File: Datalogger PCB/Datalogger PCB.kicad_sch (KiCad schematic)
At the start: 45 parts, among them J1 Conn_01x02_Pin, M1 Motor_Servo, M2 Motor_Servo, M3 Motor_Servo, M4 Motor_Servo, U1 Teensy4.1, U2 BNO055, U3 LPS25HB, U4 AMS1117-5.0, U5 NRF24L01_Breakout, U6 VN5E160STR-E, U7 VN5E160STR-E, U8 VN5E160STR-E, U9 VN5E160STR-E

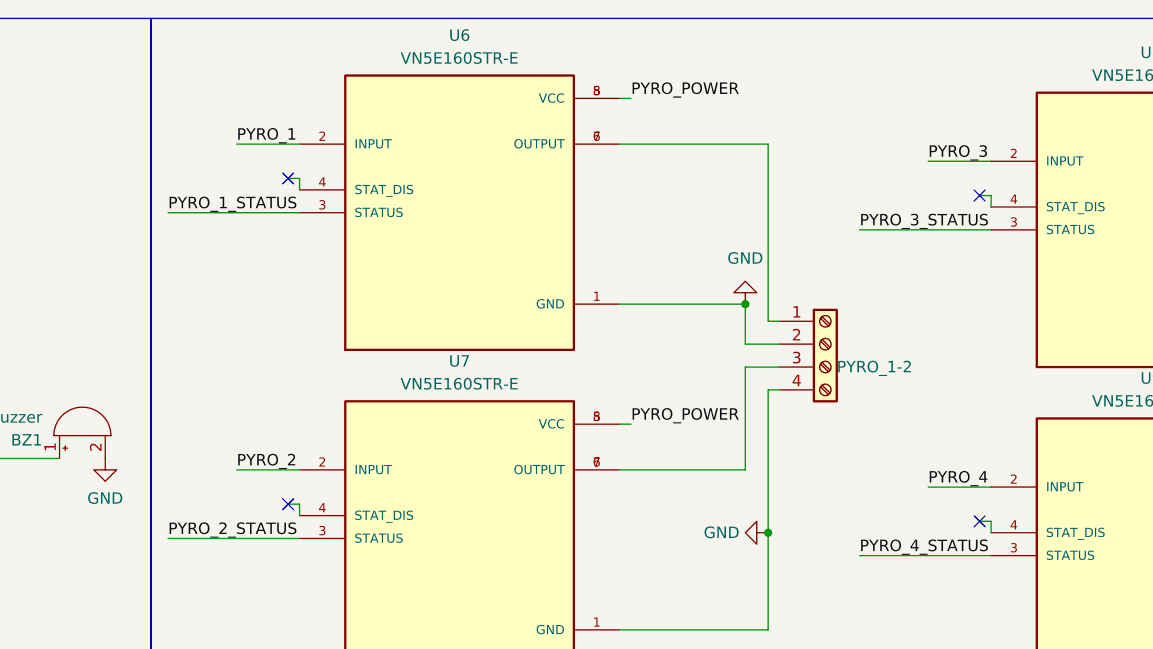
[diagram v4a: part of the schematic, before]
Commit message: Added pull down resistor to pyro channels
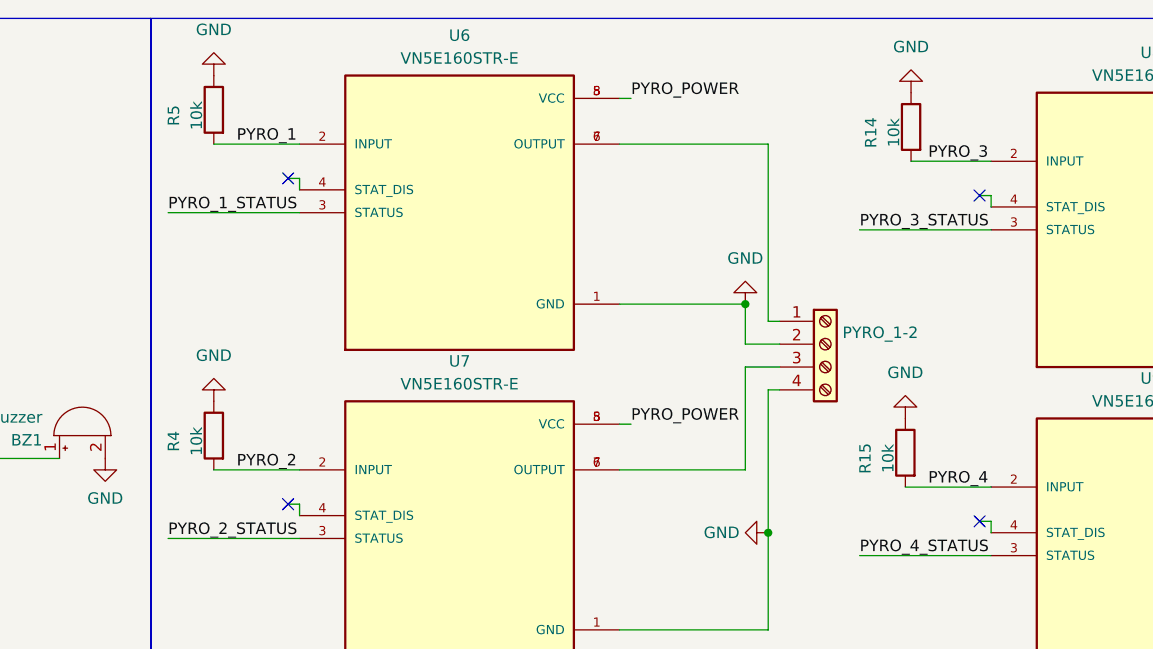
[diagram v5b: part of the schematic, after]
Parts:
- added R14, R15, R4, R5: 10k, Resistor_SMD:R_0603_1608Metric_Pad0.98x0.95mm_HandSolder, symbol Device:R
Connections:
- net GND: now also R14.1, R15.1, R4.1, R5.1
- net PYRO_1: now also R5.2
- net PYRO_2: now also R4.2
- net PYRO_3: now also R14.2
- net PYRO_4: now also R15.2
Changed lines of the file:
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@@
     (stroke (width 0) (type default))
   )
-  (wire (pts (xy 219.71 64.135) (xy 226.695 64.135))
+  (wire (pts (xy 217.17 64.135) (xy 226.695 64.135))
     (stroke (width 0) (type default))
   )
@@
     (stroke (width 0) (type default))
   )
-  (wire (pts (xy 142.875 26.035) (xy 149.86 26.035))
+  (wire (pts (xy 140.335 26.035) (xy 149.86 26.035))
     (stroke (width 0) (type default))
   )
@@
     (stroke (width 0) (type default))
   )
-  (wire (pts (xy 142.875 62.23) (xy 149.86 62.23))
+  (wire (pts (xy 140.335 62.23) (xy 149.86 62.23))
     (stroke (width 0) (type default))
   )
@@
     (stroke (width 0) (type default))
   )
-  (wire (pts (xy 219.71 27.94) (xy 226.695 27.94))
+  (wire (pts (xy 217.805 27.94) (xy 226.695 27.94))
     (stroke (width 0) (type default))
   )
@@
     )
   )
+  (symbol (lib_id "Device:R") (at 140.335 58.42 0) (mirror y) (unit 1)
+    (in_bom yes) (on_board yes) (dnp no)
+    (property "Reference" "R4" (at 135.89 59.055 90)
+      (effects (font (size 1.27 1.27)))
+    )
+    (property "Value" "10k" (at 138.43 59.055 90)
+      (effects (font (size 1.27 1.27)))
+    )
+    (property "Footprint" "Resistor_SMD:R_0603_1608Metric_Pad0.98x0.95mm_HandSolder" (at 142.113 58.42 90)
+      (effects (font (size 1.27 1.27)) hide)
+    )
+    (property "Datasheet" "~" (at 140.335 58.42 0)
+      (effects (font (size 1.27 1.27)) hide)
+    )
+    (pin "1")
+    (pin "2")
+    (instances
+      (project "Datalogger PCB"
+        (path "/a3bc5533-d6ac-45b5-a7d9-fc1b12646794"
+          (reference "R4") (unit 1)
+        )
+      )
+    )
+  )
   (symbol (lib_id "Device:R") (at 190.5 190.5 180) (unit 1)
     (in_bom yes) (on_board yes) (dnp no)
@@
     )
   )
+  (symbol (lib_id "Device:R") (at 217.805 24.13 0) (mirror y) (unit 1)
+    (in_bom yes) (on_board yes) (dnp no)
+    (property "Reference" "R14" (at 213.36 24.765 90)
+      (effects (font (size 1.27 1.27)))
+    )
+    (property "Value" "10k" (at 215.9 24.765 90)
+      (effects (font (size 1.27 1.27)))
+    )
+    (property "Footprint" "Resistor_SMD:R_0603_1608Metric_Pad0.98x0.95mm_HandSolder" (at 219.583 24.13 90)
+      (effects (font (size 1.27 1.27)) hide)
+    )
+    (property "Datasheet" "~" (at 217.805 24.13 0)
+      (effects (font (size 1.27 1.27)) hide)
+    )
+    (pin "1")
+    (pin "2")
+    (instances
+      (project "Datalogger PCB"
+        (path "/a3bc5533-d6ac-45b5-a7d9-fc1b12646794"
+          (reference "R14") (unit 1)
+        )
+      )
+    )
+  )
   (symbol (lib_id "VN5E160STR-E:VN5E160STR-E") (at 244.475 71.755 0) (unit 1)
     (in_bom yes) (on_board yes) (dnp no)
@@
     )
   )
+  (symbol (lib_id "Device:R") (at 217.17 60.325 0) (mirror y) (unit 1)
+    (in_bom yes) (on_board yes) (dnp no)
+    (property "Reference" "R15" (at 212.725 60.96 90)
+      (effects (font (size 1.27 1.27)))
+    )
+    (property "Value" "10k" (at 215.265 60.96 90)
+      (effects (font (size 1.27 1.27)))
+    )
+    (property "Footprint" "Resistor_SMD:R_0603_1608Metric_Pad0.98x0.95mm_HandSolder" (at 218.948 60.325 90)
+      (effects (font (size 1.27 1.27)) hide)
+    )
+    (property "Datasheet" "~" (at 217.17 60.325 0)
+      (effects (font (size 1.27 1.27)) hide)
+    )
+    (pin "1")
+    (pin "2")
+    (instances
+      (project "Datalogger PCB"
+        (path "/a3bc5533-d6ac-45b5-a7d9-fc1b12646794"
+          (reference "R15") (unit 1)
+        )
+      )
+    )
+  )
   (symbol (lib_id "Motor:Motor_Servo") (at 317.5 87.63 0) (unit 1)
     (in_bom yes) (on_board yes) (dnp no) (fields_autoplaced)
@@
     )
   )
+  (symbol (lib_id "power:GND") (at 140.335 54.61 180) (unit 1)
+    (in_bom yes) (on_board yes) (dnp no) (fields_autoplaced)
+    (property "Reference" "#PWR04" (at 140.335 48.26 0)
+      (effects (font (size 1.27 1.27)) hide)
+    )
+    (property "Value" "GND" (at 140.335 49.53 0)
+      (effects (font (size 1.27 1.27)))
+    )
+    (property "Footprint" "" (at 140.335 54.61 0)
+      (effects (font (size 1.27 1.27)) hide)
+    )
+    (property "Datasheet" "" (at 140.335 54.61 0)
+      (effects (font (size 1.27 1.27)) hide)
+    )
+    (pin "1")
+    (instances
+      (project "Datalogger PCB"
+        (path "/a3bc5533-d6ac-45b5-a7d9-fc1b12646794"
+          (reference "#PWR04") (unit 1)
+        )
+      )
+    )
+  )
   (symbol (lib_id "power:+3.3V") (at 89.535 43.18 270) (unit 1)
     (in_bom yes) (on_board yes) (dnp no) (fields_autoplaced)
@@
   (symbol (lib_id "Connector:Screw_Terminal_01x04") (at 208.28 48.26 0) (unit 1)
     (in_bom yes) (on_board yes) (dnp no)
-    (property "Reference" "PYRO_1-2" (at 209.55 50.8 0)
+    (property "Reference" "PYRO_1-2" (at 210.185 46.99 0)
       (effects (font (size 1.27 1.27)) (justify left))
     )
@@
     )
   )
+  (symbol (lib_id "power:GND") (at 217.17 56.515 180) (unit 1)
+    (in_bom yes) (on_board yes) (dnp no) (fields_autoplaced)
+    (property "Reference" "#PWR053" (at 217.17 50.165 0)
+      (effects (font (size 1.27 1.27)) hide)
+    )
+    (property "Value" "GND" (at 217.17 51.435 0)
+      (effects (font (size 1.27 1.27)))
+    )
+    (property "Footprint" "" (at 217.17 56.515 0)
+      (effects (font (size 1.27 1.27)) hide)
+    )
+    (property "Datasheet" "" (at 217.17 56.515 0)
+      (effects (font (size 1.27 1.27)) hide)
+    )
+    (pin "1")
+    (instances
+      (project "Datalogger PCB"
+        (path "/a3bc5533-d6ac-45b5-a7d9-fc1b12646794"
+          (reference "#PWR053") (unit 1)
+        )
+      )
+    )
+  )
   (symbol (lib_id "power:+3.3V") (at 86.36 177.8 180) (unit 1)
     (in_bom yes) (on_board yes) (dnp no) (fields_autoplaced)
@@
         )
       )
+    )
+  )
+  (symbol (lib_id "power:GND") (at 217.805 20.32 180) (unit 1)
+    (in_bom yes) (on_board yes) (dnp no) (fields_autoplaced)
+    (property "Reference" "#PWR052" (at 217.805 13.97 0)
+      (effects (font (size 1.27 1.27)) hide)
+    )
+    (property "Value" "GND" (at 217.805 15.24 0)
+      (effects (font (size 1.27 1.27)))
+    )
+    (property "Footprint" "" (at 217.805 20.32 0)
+      (effects (font (size 1.27 1.27)) hide)
+    )
+    (property "Datasheet" "" (at 217.805 20.32 0)
+      (effects (font (size 1.27 1.27)) hide)
+    )
+    (pin "1")
+    (instances
+      (project "Datalogger PCB"
+        (path "/a3bc5533-d6ac-45b5-a7d9-fc1b12646794"
+          (reference "#PWR052") (unit 1)
+        )
+      )
+    )
+  )
+  (symbol (lib_id "Device:R") (at 140.335 22.225 0) (mirror y) (unit 1)
+    (in_bom yes) (on_board yes) (dnp no)
+    (property "Reference" "R5" (at 135.89 22.86 90)
+      (effects (font (size 1.27 1.27)))
+    )
+    (property "Value" "10k" (at 138.43 22.86 90)
+      (effects (font (size 1.27 1.27)))
+    )
+    (property "Footprint" "Resistor_SMD:R_0603_1608Metric_Pad0.98x0.95mm_HandSolder" (at 142.113 22.225 90)
+      (effects (font (size 1.27 1.27)) hide)
+    )
+    (property "Datasheet" "~" (at 140.335 22.225 0)
+      (effects (font (size 1.27 1.27)) hide)
+    )
+    (pin "1")
+    (pin "2")
+    (instances
+      (project "Datalogger PCB"
+        (path "/a3bc5533-d6ac-45b5-a7d9-fc1b12646794"
+          (reference "R5") (unit 1)
+        )
+      )
+    )
+  )
+  (symbol (lib_id "power:GND") (at 140.335 18.415 180) (unit 1)
+    (in_bom yes) (on_board yes) (dnp no) (fields_autoplaced)
+    (property "Reference" "#PWR08" (at 140.335 12.065 0)
+      (effects (font (size 1.27 1.27)) hide)
+    )
+    (property "Value" "GND" (at 140.335 13.335 0)
+      (effects (font (size 1.27 1.27)))
+    )
+    (property "Footprint" "" (at 140.335 18.415 0)
+      (effects (font (size 1.27 1.27)) hide)
+    )
+    (property "Datasheet" "" (at 140.335 18.415 0)
+      (effects (font (size 1.27 1.27)) hide)
+    )
+    (pin "1")
+    (instances
+      (project "Datalogger PCB"
+        (path "/a3bc5533-d6ac-45b5-a7d9-fc1b12646794"
+          (reference "#PWR08") (unit 1)
+        )
+      )

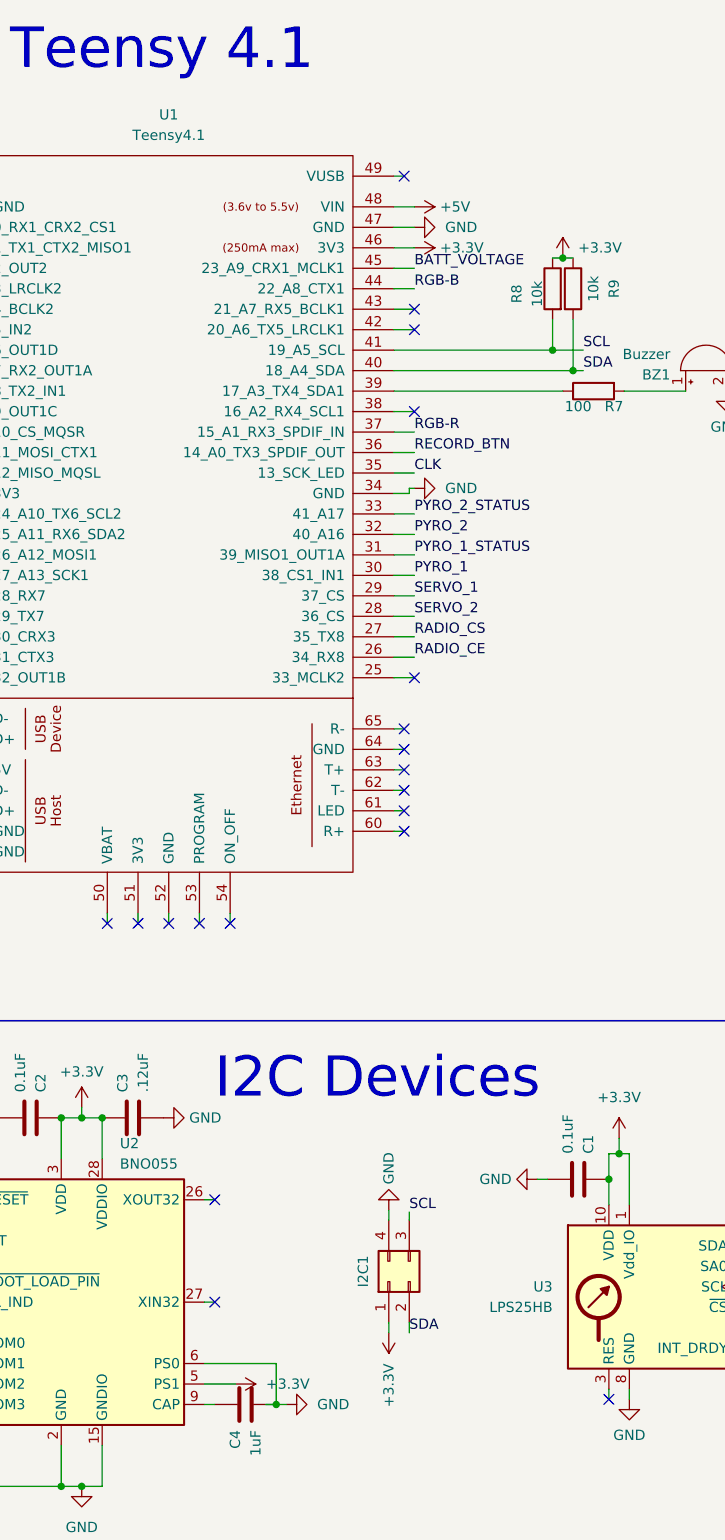
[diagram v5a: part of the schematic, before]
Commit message: Fixed a couple of pcb errors
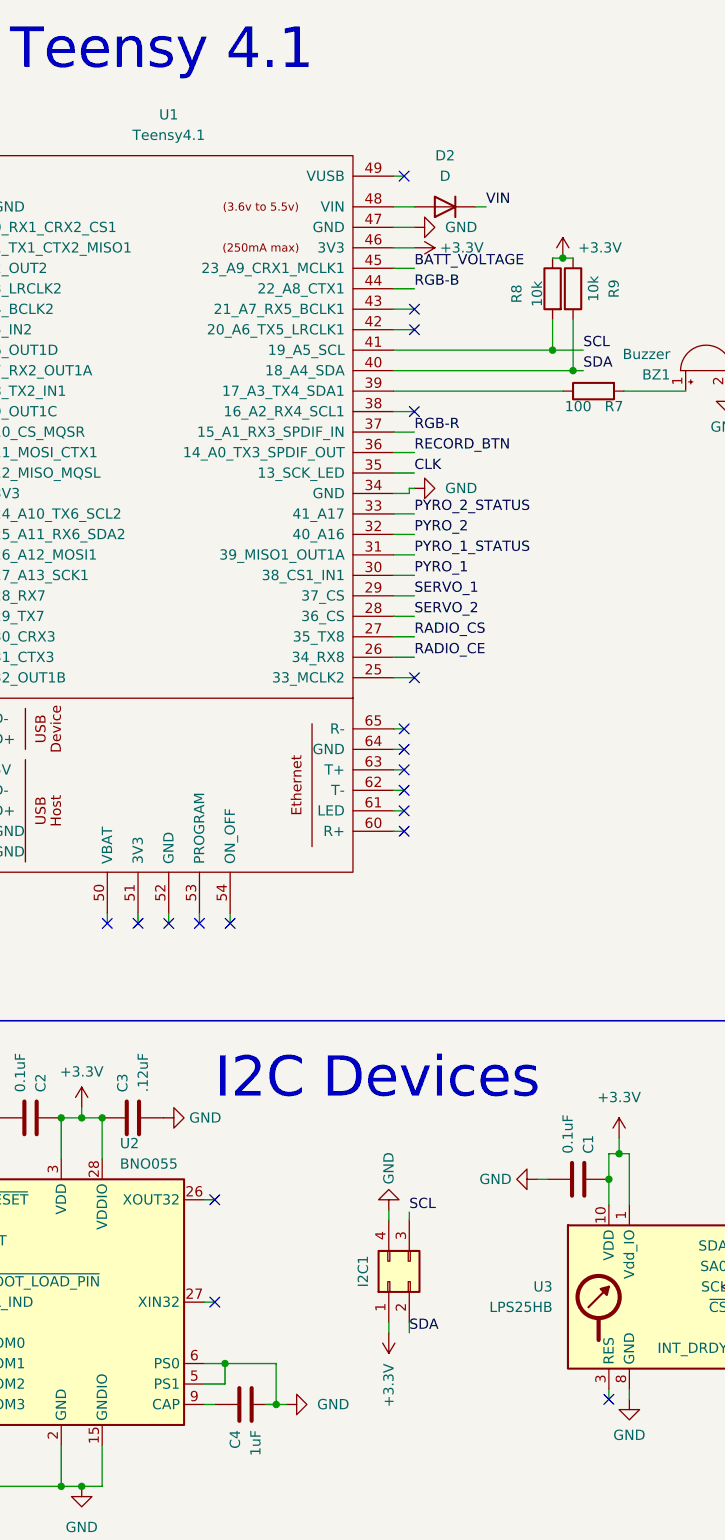
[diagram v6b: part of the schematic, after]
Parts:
- added D2: D, Diode_SMD:D_0603_1608Metric_Pad1.05x0.95mm_HandSolder, symbol Device:D
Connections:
- net +3.3V: no longer U2.5 (PS1)
- net +5V: no longer U1.48 (VIN)
- net GND: now also U2.5 (PS1)
- net VIN: now also D2.1 (K)
- new net: D2.2 (A), U1.48 (VIN)
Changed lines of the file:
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@@
   (junction (at 50.8 151.13) (diameter 0) (color 0 0 0 0)
   )
+  (junction (at 66.04 181.61) (diameter 0) (color 0 0 0 0)
+  )
   (junction (at 223.52 184.785) (diameter 0) (color 0 0 0 0)
   )
@@
     (stroke (width 0) (type default))
   )
-  (wire (pts (xy 63.5 181.61) (xy 72.39 181.61))
+  (wire (pts (xy 63.5 181.61) (xy 66.04 181.61))
     (stroke (width 0) (type default))
   )
@@
     (stroke (width 0) (type default))
   )
-  (wire (pts (xy 67.31 184.15) (xy 63.5 184.15))
-    (stroke (width 0) (type default))
-  )
   (wire (pts (xy 113.665 161.925) (xy 113.665 158.75))
     (stroke (width 0) (type default))
@@
     (stroke (width 0) (type default))
   )
+  (wire (pts (xy 66.04 181.61) (xy 72.39 181.61))
+    (stroke (width 0) (type default))
+  )
   (wire (pts (xy 89.535 88.9) (xy 86.995 88.9))
     (stroke (width 0) (type default))
@@
     (stroke (width 0) (type default))
   )
+  (wire (pts (xy 66.04 184.15) (xy 66.04 181.61))
+    (stroke (width 0) (type default))
+  )
   (wire (pts (xy 29.845 60.96) (xy 31.115 60.96))
     (stroke (width 0) (type default))
@@
     (stroke (width 0) (type default))
   )
+  (wire (pts (xy 63.5 184.15) (xy 66.04 184.15))
+    (stroke (width 0) (type default))
+  )
+  (wire (pts (xy 98.425 38.1) (xy 97.155 38.1))
+    (stroke (width 0) (type default))
+  )
   (wire (pts (xy 148.59 66.04) (xy 149.86 66.04))
     (stroke (width 0) (type default))
@@
     (effects (font (size 1.27 1.27)) (justify left bottom))
   )
+  (label "VIN" (at 98.425 38.1 0) (fields_autoplaced)
+    (effects (font (size 1.27 1.27)) (justify left bottom))
+  )
   (label "RADIO_CE" (at 89.535 93.98 0) (fields_autoplaced)
     (effects (font (size 1.27 1.27)) (justify left bottom))
@@
     )
   )
-  (symbol (lib_id "power:+5V") (at 89.535 38.1 270) (unit 1)
-    (in_bom yes) (on_board yes) (dnp no) (fields_autoplaced)
-    (property "Reference" "#PWR043" (at 85.725 38.1 0)
-      (effects (font (size 1.27 1.27)) hide)
-    )
-    (property "Value" "+5V" (at 92.71 38.1 90)
-      (effects (font (size 1.27 1.27)) (justify left))
-    )
-    (property "Footprint" "" (at 89.535 38.1 0)
-      (effects (font (size 1.27 1.27)) hide)
-    )
-    (property "Datasheet" "" (at 89.535 38.1 0)
-      (effects (font (size 1.27 1.27)) hide)
-    )
-    (pin "1")
-    (instances
-      (project "Datalogger PCB"
-        (path "/a3bc5533-d6ac-45b5-a7d9-fc1b12646794"
-          (reference "#PWR043") (unit 1)
-        )
-      )
-    )
-  )
   (symbol (lib_id "power:+5V") (at 224.79 184.785 270) (unit 1)
     (in_bom yes) (on_board yes) (dnp no) (fields_autoplaced)
@@
     )
   )
-  (symbol (lib_id "power:+3.3V") (at 67.31 184.15 270) (unit 1)
-    (in_bom yes) (on_board yes) (dnp no) (fields_autoplaced)
-    (property "Reference" "#PWR027" (at 63.5 184.15 0)
-      (effects (font (size 1.27 1.27)) hide)
-    )
-    (property "Value" "+3.3V" (at 71.12 184.15 90)
-      (effects (font (size 1.27 1.27)) (justify left))
-    )
-    (property "Footprint" "" (at 67.31 184.15 0)
-      (effects (font (size 1.27 1.27)) hide)
-    )
-    (property "Datasheet" "" (at 67.31 184.15 0)
-      (effects (font (size 1.27 1.27)) hide)
-    )
-    (pin "1")
-    (instances
-      (project "Datalogger PCB"
-        (path "/a3bc5533-d6ac-45b5-a7d9-fc1b12646794"
-          (reference "#PWR027") (unit 1)
-        )
-      )
-    )
-  )
   (symbol (lib_id "power:GND") (at 21.59 37.465 0) (unit 1)
     (in_bom yes) (on_board yes) (dnp no) (fields_autoplaced)
@@
         )
       )
+    )
+  )
+  (symbol (lib_id "Device:D") (at 93.345 38.1 180) (unit 1)
+    (in_bom yes) (on_board yes) (dnp no) (fields_autoplaced)
+    (property "Reference" "D2" (at 93.345 31.75 0)
+      (effects (font (size 1.27 1.27)))
+    )
+    (property "Value" "D" (at 93.345 34.29 0)
+      (effects (font (size 1.27 1.27)))
+    )
+    (property "Footprint" "Diode_SMD:D_0603_1608Metric_Pad1.05x0.95mm_HandSolder" (at 93.345 38.1 0)
+      (effects (font (size 1.27 1.27)) hide)
+    )
+    (property "Datasheet" "~" (at 93.345 38.1 0)
+      (effects (font (size 1.27 1.27)) hide)
+    )
+    (property "Sim.Device" "D" (at 93.345 38.1 0)
+      (effects (font (size 1.27 1.27)) hide)
+    )
+    (property "Sim.Pins" "1=K 2=A" (at 93.345 38.1 0)
+      (effects (font (size 1.27 1.27)) hide)
+    )
+    (pin "2")
+    (pin "1")
+    (instances
+      (project "Datalogger PCB"
+        (path "/a3bc5533-d6ac-45b5-a7d9-fc1b12646794"
+          (reference "D2") (unit 1)
+        )
+      )
